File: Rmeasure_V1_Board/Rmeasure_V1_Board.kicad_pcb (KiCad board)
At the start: 2 copper layers, 82.4 x 28.6 mm, 58 parts, among them J1 SWD, J2 USB_B_Micro, J3 CON_CAN, J4 CON_CAN, SW1 RST, SW2 BOOT, U1 STM32F042K6Tx, U2 NCP1117-3.3_SOT223, U3 SN65HVD232, U4 FT230XQ, Y1 8MHz

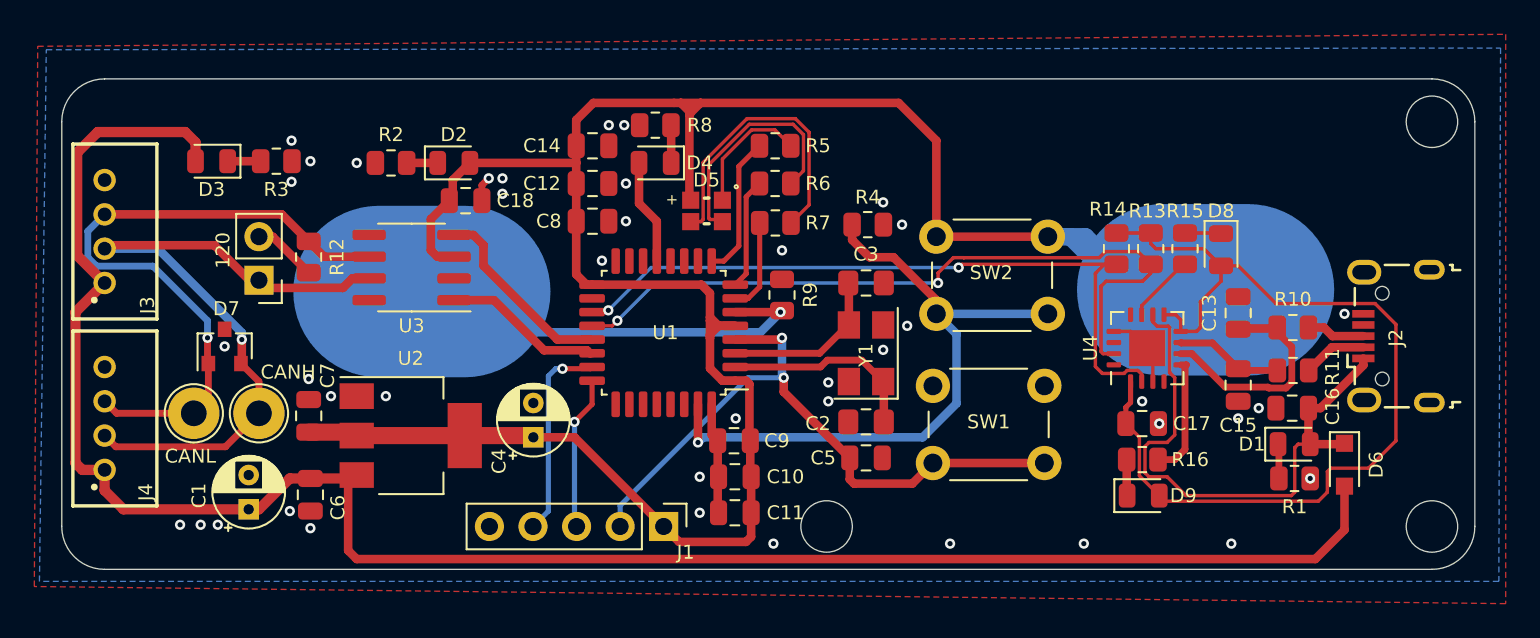
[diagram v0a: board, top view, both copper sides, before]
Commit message: Add Rmeasure, Teensy AX12 and main PCB for the CDR2022
-Rmeasure put in production on 13/10
-Add UART to main pcb and rerouting can bus and swap tx/rx pin for the XBEE
-new pcb with teensy 3.2, AX-12 connectivity, UART and CANbus
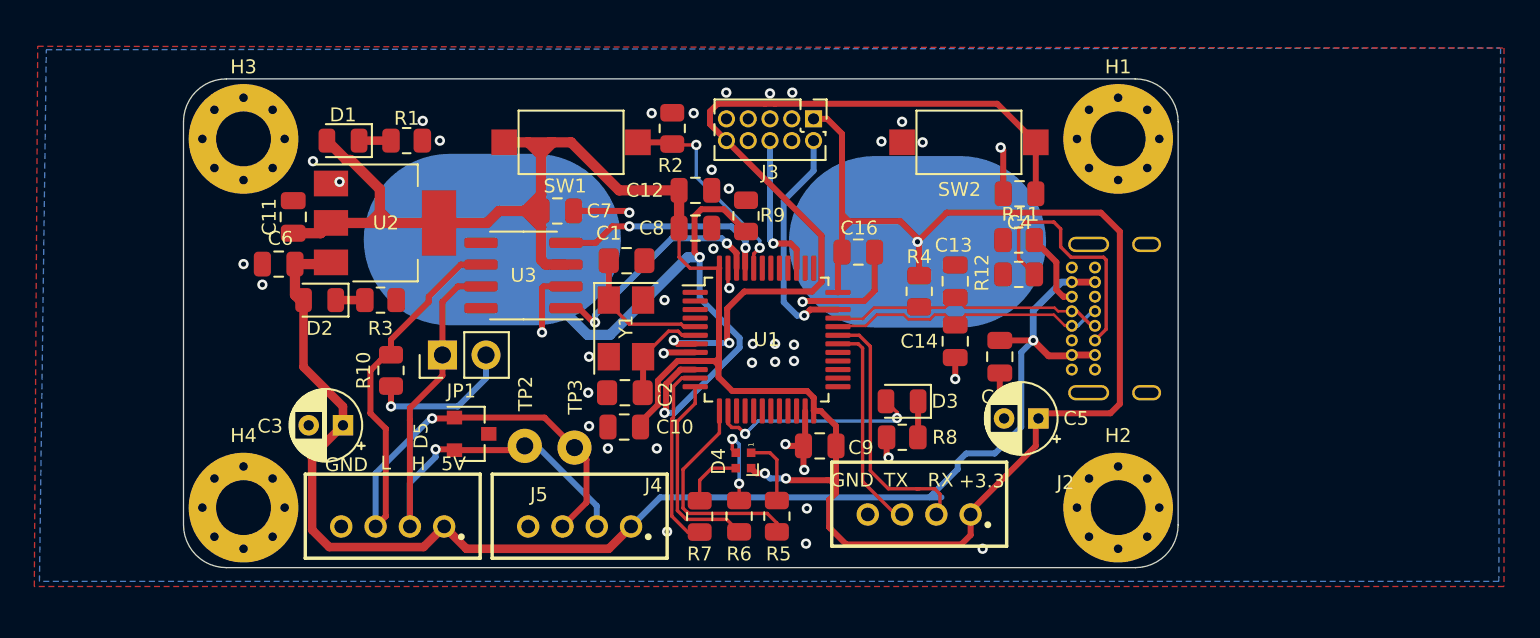
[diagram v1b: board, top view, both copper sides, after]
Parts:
- removed 120: JUMPER, Connector_PinHeader_2.54mm:PinHeader_1x02_P2.54mm_Vertical
- removed C17, C18: 100n, Capacitor_SMD:C_0805_2012Metric
- removed CANH, CANL: TestPoint, TestPoint:TestPoint_Loop_D2.54mm_Drill1.5mm_Beaded
- removed D6: DIODE, Diode_SMD:D_SOD-323_HandSoldering
- removed D7: TVS, Package_TO_SOT_SMD:SOT-23
- removed D8: LED_TX, LED_SMD:LED_0805_2012Metric
- removed D9: LED_RX, LED_SMD:LED_0805_2012Metric
- removed R13, R14: 10k, Resistor_SMD:R_0805_2012Metric
- removed R15, R16: 270, Resistor_SMD:R_0805_2012Metric
- removed U4: FT230XQ, Package_DFN_QFN:QFN-16-1EP_4x4mm_P0.65mm_EP2.1x2.1mm
- added H1: MountingHole_Pad, MountingHole:MountingHole_3.2mm_M3_Pad_Via, F.Cu at (121.9, 81.5)
- added H2: MountingHole_Pad, MountingHole:MountingHole_3.2mm_M3_Pad_Via, F.Cu at (121.9, 103.0)
- added H3: MountingHole_Pad, MountingHole:MountingHole_3.2mm_M3_Pad_Via, F.Cu at (70.9, 81.5)
- added H4: MountingHole_Pad, MountingHole:MountingHole_3.2mm_M3_Pad_Via, F.Cu at (70.9, 103.0)
- added J5: CON_CAN, AREA_lib_Connector:Wuerth_2mm_4pin_62000411622, F.Cu at (79.6, 103.5)
- added JP1: JUMPER, Connector_PinHeader_2.54mm:PinHeader_1x02_P2.54mm_Vertical, F.Cu at (82.5, 94.1)
- added TP2: TestPoint, TestPoint:TestPoint_Loop_D1.80mm_Drill1.0mm_Beaded, F.Cu at (87.3, 99.4)
- added TP3: TestPoint, TestPoint:TestPoint_Loop_D1.80mm_Drill1.0mm_Beaded, F.Cu at (90.2, 99.5)
- C1: value 10u -> 18p; footprint Capacitor_THT:CP_Radial_D4.0mm_P2.00mm -> Capacitor_SMD:C_0805_2012Metric_Pad1.18x1.45mm_HandSolder
- C12, C16, C7: value 10u -> 100n
- C14: value 10u -> 47p
- C15: value 47p -> 10u
- C3: value 18p -> 10u; footprint Capacitor_SMD:C_0805_2012Metric_Pad1.18x1.45mm_HandSolder -> Capacitor_THT:CP_Radial_D4.0mm_P2.00mm
- C4: value 10u -> 0.1u; footprint Capacitor_THT:CP_Radial_D4.0mm_P2.00mm -> Capacitor_SMD:C_0805_2012Metric
- C5: value 0.1u -> 10u; footprint Capacitor_SMD:C_0805_2012Metric -> Capacitor_THT:CP_Radial_D4.0mm_P2.00mm
- C8: value 100n -> 10u
- D1: value LED_5Vusb -> LED_33V
- D2: value LED_33V -> LED_5V
- D3: value LED_5V -> LED_DEBUG
- D4: value LED_DEBUG -> LED_RGBA; footprint LED_SMD:LED_0805_2012Metric -> LED_SMD:LED_SK6812_EC15_1.5x1.5mm
- D5: value LED_RGBA -> TVS; footprint AREA_lib_composant:WL-SFCW_0805 -> Package_TO_SOT_SMD:SOT-23
- J1: value SWD -> USB_C_Receptacle_USB2.0; footprint Connector_PinHeader_2.54mm:PinHeader_1x05_P2.54mm_Vertical -> Connector_USB:USB_C_Receptacle_GCT_USB4085; moved to B.Cu
- J2: value USB_B_Micro -> CON_debug; footprint Connector_USB:USB_Micro-B_Wuerth_629105150521 -> AREA_lib_Connector:Wuerth_2mm_4pin_62000411622
- J3: value CON_CAN -> Conn_ARM_JTAG_SWD_10; footprint AREA_lib_Connector:Wuerth_2mm_4pin_62000411622 -> Connector_PinHeader_1.27mm:PinHeader_2x05_P1.27mm_Vertical
- R10: value 270 -> 120
- R11: value 270 -> 5.1k
- R12: value 120 -> 5.1k
- R2: value 270 -> 10k
- R4: value 10k -> 1.5k
- SW1: value RST -> BOOT; footprint Button_Switch_THT:SW_PUSH_6mm_H5mm -> Button_Switch_SMD:SW_SPST_CK_RS282G05A3
- SW2: value BOOT -> RST; footprint Button_Switch_THT:SW_PUSH_6mm_H5mm -> Button_Switch_SMD:SW_SPST_CK_RS282G05A3
- U1: value STM32F042K6Tx -> STM32F302C6Tx; footprint Package_QFP:LQFP-32_7x7mm_P0.8mm -> Package_QFP:LQFP-48_7x7mm_P0.5mm
- moved D1 58.2 mm to (76.7, 81.6), turned to 180 degrees
- moved R1 55.4 mm to (80.4, 81.6)
- moved R10 52.6 mm to (79.5, 95.0), turned to 270 degrees
- moved D3 42.6 mm to (109.3, 96.8)
- moved R12 41.4 mm to (116.1, 89.4), turned to 180 degrees
- moved J3 41.3 mm to (104.1, 80.3)
- moved C4 31.7 mm to (116.2, 84.7), turned to 180 degrees
- moved C3 31.6 mm to (76.7, 98.2), turned to 180 degrees
- moved C11 31.0 mm to (73.8, 86.0), turned to 90 degrees
- moved J2 29.5 mm to (110.3, 102.8), turned to 0 degrees
- moved J1 28.2 mm to (119.2, 89.0)
- moved J4 27.7 mm to (90.5, 103.5), turned to 0 degrees
- moved C16 26.9 mm to (106.8, 88.1), turned to 0 degrees
- moved C1 26.4 mm to (93.2, 88.6), turned to 0 degrees
- moved SW1 25.4 mm to (90.0, 81.7)
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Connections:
- C1 pad 1: +5V -> Net-(C1-Pad1)
- C14 pad 1: +3V3 -> /USB-
- C15 pad 1: /USB- -> +5V
- C16 pad 1: /5Vusb -> +3V3
- C3 pad 1: Net-(C3-Pad1) -> +5V
- C4 pad 1: +3V3 -> /RST
- C5 pad 1: /RST -> +3V3
- D1 pad 2: /5Vusb -> +3V3
- D2 pad 2: +3V3 -> +5V
- D3 pad 2: +5V -> Net-(D3-Pad2)
- D5 pad 1: Net-(D5-Pad1) -> /CANL
- D5 pad 2: Net-(D5-Pad2) -> /CANH
- D5 pad 3: Net-(D5-Pad3) -> GND
- J2 pad 1: /5Vusb -> +3V3
- J2 pad 2: Net-(J2-Pad2) -> /RX
- J2 pad 3: Net-(J2-Pad3) -> /TX
- J2 pad 4: Net-(J2-Pad4) -> GND
- J3 pad 1: +5V -> +3V3
- J3 pad 2: /CANH -> /SWDIO
- J3 pad 3: /CANL -> GND
- J3 pad 4: GND -> /CLK
- R10 pad 1: /USB+ -> /CANL
- R10 pad 2: Net-(J2-Pad3) -> Net-(JP1-Pad2)
- R11 pad 1: /USB- -> Net-(J1-PadA5)
- R11 pad 2: Net-(J2-Pad2) -> GND
- R12 pad 1: /CANL -> Net-(J1-PadB5)
- R12 pad 2: Net-(JP1-Pad2) -> GND
- R2 pad 2: Net-(D2-Pad1) -> /BOOT0
- R3 pad 2: Net-(D3-Pad1) -> Net-(D2-Pad1)
- R4 pad 1: GND -> +3V3
- R4 pad 2: Net-(R4-Pad2) -> /USB+
- R5 pad 1: Net-(D5-Pad1) -> Net-(D4-Pad1)
- R6 pad 1: Net-(D5-Pad2) -> Net-(D4-Pad2)
- R7 pad 1: Net-(D5-Pad3) -> Net-(D4-Pad3)
- R8 pad 2: Net-(D4-Pad1) -> Net-(D3-Pad1)
- SW1 pad 1: GND -> +3V3
- SW1 pad 2: /RST -> /BOOT0
- SW2 pad 1: +3V3 -> GND
- SW2 pad 2: Net-(R4-Pad2) -> /RST
- U1 pad 1: +3V3 -> Net-(U1-Pad1)
- U1 pad 10: Net-(U1-Pad10) -> /R_point
- U1 pad 11: Net-(U1-Pad11) -> /Rouge
- U1 pad 12: Net-(U1-Pad12) -> /Vert
- U1 pad 13: Net-(D4-Pad2) -> /Bleu
- U1 pad 14: Net-(U1-Pad14) -> Net-(D3-Pad2)
- U1 pad 16: GND -> Net-(U1-Pad16)
- U1 pad 17: +3V3 -> Net-(U1-Pad17)
- U1 pad 19: /RX -> Net-(U1-Pad19)
- U1 pad 2: Net-(C2-Pad1) -> Net-(U1-Pad2)
- U1 pad 20: /TX -> Net-(U1-Pad20)
- U1 pad 21: /CANRX -> Net-(U1-Pad21)
- U1 pad 22: /CANTX -> Net-(U1-Pad22)
- U1 pad 23: /SWDIO -> GND
- U1 pad 24: /CLK -> +3V3
- U1 pad 3: Net-(C3-Pad1) -> Net-(U1-Pad3)
- U1 pad 30: Net-(U1-Pad30) -> /TX
- U1 pad 31: Net-(R4-Pad2) -> /RX
- U1 pad 32: GND -> /USB-
- U1 pad 4: /RST -> Net-(U1-Pad4)
- U1 pad 5: +3V3 -> Net-(C1-Pad1)
- U1 pad 6: /R_point -> Net-(C2-Pad1)
- U1 pad 7: /Rouge -> /RST
- U1 pad 8: /Vert -> GND
- U1 pad 9: /Bleu -> +3V3
- Y1 pad 1: Net-(C2-Pad1) -> Net-(C1-Pad1)
- Y1 pad 3: Net-(C3-Pad1) -> Net-(C2-Pad1)
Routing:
- net Net-(C17-Pad1): track 56.4 -> 0.00 mm
- net Net-(R4-Pad2): track 38.5 -> 0.00 mm, vias 1 -> 0
- net /5Vusb: track 33.2 -> 0.00 mm
- net /TX: track 43.4 -> 12.1 mm, vias 2 -> 0
- net +5V: track 113.4 -> 83.7 mm, vias 0 -> 1
- net /RX: track 42.1 -> 15.4 mm, vias 2 -> 0
- net +3V3: track 134.1 -> 155.4 mm, vias 0 -> 3
- net Net-(D5-Pad3): track 17.4 -> 0.00 mm
- net GND: track 12.4 -> 29.6 mm, vias 41 -> 44
- net Net-(J1-PadB5): track 0.00 -> 14.8 mm
- net Net-(D5-Pad2): track 13.9 -> 0.00 mm
- net /R_point: track 25.1 -> 38.5 mm, vias 1 -> 2
- net Net-(D3-Pad2): track 0.00 -> 12.5 mm, vias 0 -> 2
- net /BOOT0: track 0.00 -> 12.3 mm, vias 0 -> 2
- net /USB-: track 6.31 -> 16.6 mm
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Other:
- board size 82.4 x 28.6 mm -> 58 x 28.5 mm
- board text added: "+3.3"
- board text added: "5V"
- board text added: "GND"
- board text added: "H"
- board text added: "L"
- board text added: "RX"
- board text added: "TX"

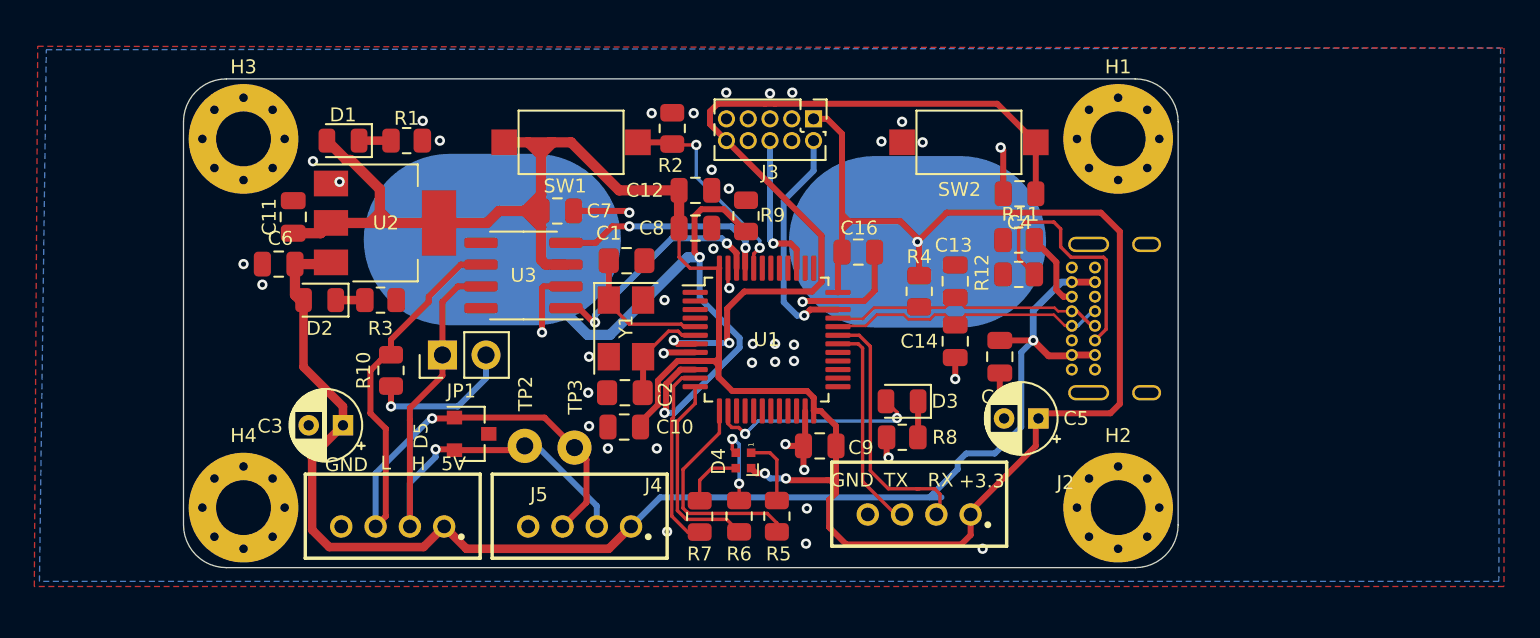
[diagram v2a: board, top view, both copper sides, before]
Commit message: change rgb on rmeasure + add library component
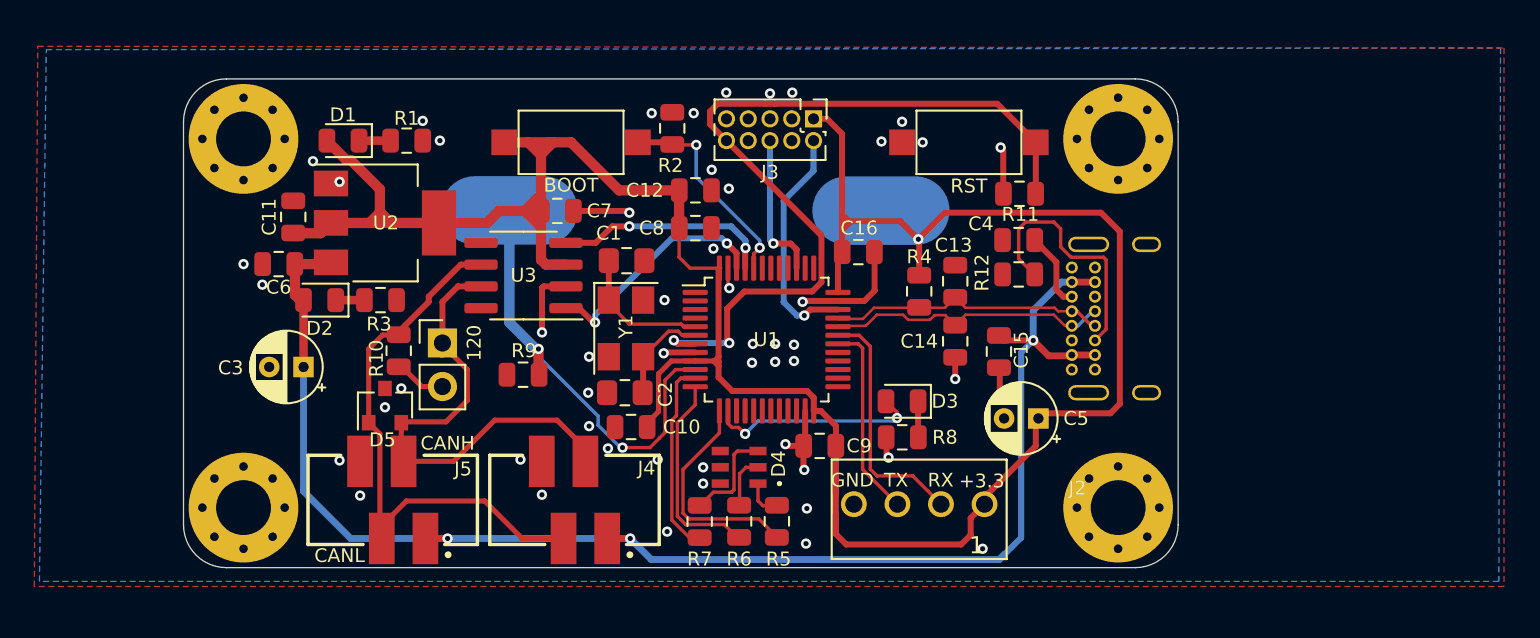
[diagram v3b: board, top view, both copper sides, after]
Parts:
- removed TP2, TP3: TestPoint, TestPoint:TestPoint_Loop_D1.80mm_Drill1.0mm_Beaded
- D4: value LED_RGBA -> LED_RGB; footprint LED_SMD:LED_SK6812_EC15_1.5x1.5mm -> AREA_lib_composant:LED_RGB_LTRBRASF6B6C011200R18
- J2: footprint AREA_lib_Connector:Wuerth_2mm_4pin_62000411622 -> AREA_lib_Connector:Wuerth_2.54mm_4pins_61900411121
- J4, J5: footprint AREA_lib_Connector:Wuerth_2mm_4pin_62000411622 -> AREA_lib_Connector:690367290476
- moved R9 16.0 mm to (87.2, 95.2), turned to 0 degrees
- moved D5 5.31 mm to (79.2, 97.0), turned to 90 degrees
- moved C3 4.10 mm to (74.4, 94.8)
- moved R10 1.23 mm to (80.0, 93.8)
- moved J4 1.00 mm to (90.2, 102.5)
- moved J5 0.95 mm to (79.6, 102.5)
- moved 120 0.70 mm to (82.5, 93.4), turned to 0 degrees
- moved D4 0.47 mm to (99.8, 100.7), turned to 90 degrees
- moved C10 0.40 mm to (93.5, 98.3)
- moved C15 0.30 mm to (115.0, 93.9)
- moved R5 0.30 mm to (102.0, 103.8)
- moved R6 0.30 mm to (99.8, 103.8)
- moved R7 0.30 mm to (97.5, 103.8)
- renumbered JP1 to 120, SW1 to BOOT, SW2 to RST
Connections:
- D4 pad 4: +3V3 -> GND
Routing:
- net /R_point: track 38.5 -> 26.1 mm
- net /CANL: track 41.7 -> 33.1 mm, vias 1 -> 0
- net +3V3: track 155.4 -> 147.9 mm, vias 3 -> 1
- net Net-(JP1-Pad2): track 8.77 -> 3.04 mm, vias 1 -> 0
- net /CANH: track 33.1 -> 29.4 mm, vias 1 -> 0
- net +5V: track 83.7 -> 86.3 mm, vias 1 -> 3
- net Net-(D4-Pad3): track 3.59 -> 5.93 mm
- net Net-(D4-Pad1): track 4.05 -> 2.22 mm
- net Net-(D4-Pad2): track 4.69 -> 3.10 mm, vias 2 -> 0
- net /RX: track 15.4 -> 14.3 mm
- net /TX: track 12.1 -> 11.5 mm
- net GND: vias 44 -> 52
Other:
- board text added: "CANH"
- board text added: "CANL"
- board text removed: "5V"
- board text removed: "H"
- board text removed: "L"
